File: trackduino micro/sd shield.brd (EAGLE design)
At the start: 43.7 x 19.6 mm, 12 parts, among them U1 FT232RL-BASICSSOP

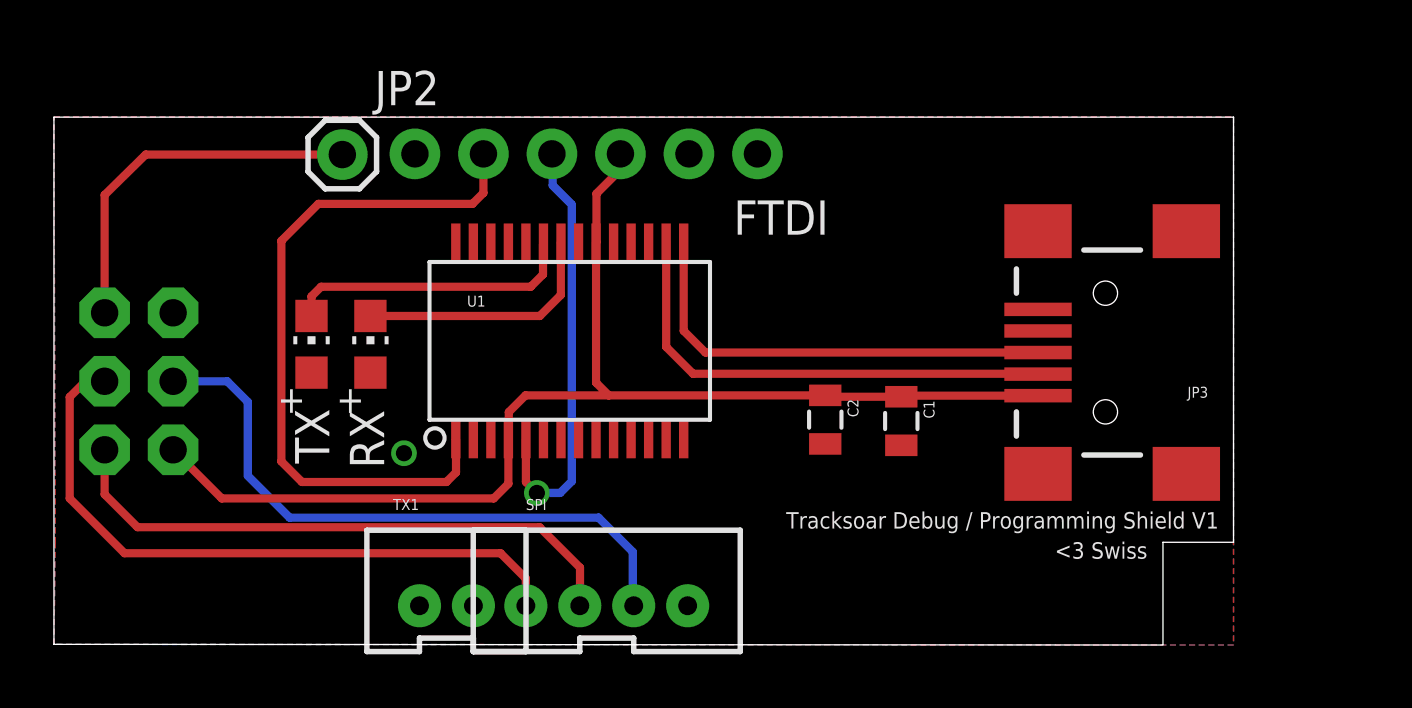
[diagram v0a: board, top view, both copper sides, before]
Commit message: Shield Updates
added sd storage shield, added fetid chip to programming shield. Moved
test boards to correct folder.
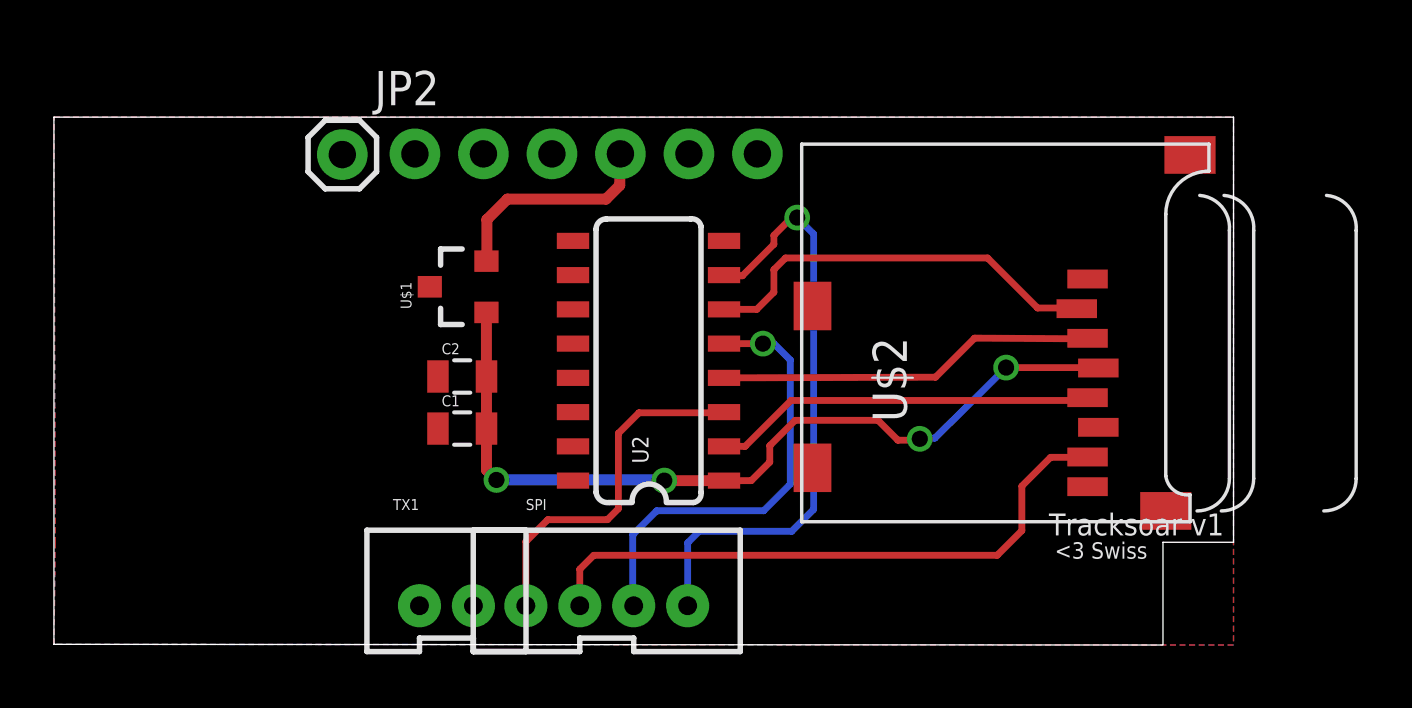
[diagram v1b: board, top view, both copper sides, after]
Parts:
- removed ICSP: AVR_SPI_PRG_6PTH, SparkFun-Connectors:2X3
- removed JP3: USBSMD, SparkFun-Connectors:USB-MINIB
- removed RX, TX: (no value), adafruit:CHIP-LED0805
- removed U1: FT232RL-BASICSSOP, SparkFun-DigitalIC:SSOP28DB
- added U$1: LM3480IM4, SparkFun-PowerIC:SOT23-3
- added U$2: MICROSD, adafruit:MICROSD
- added U2: HEX_CONVERTER, SparkFun-DigitalIC:SO016
- C2: value 100pf -> .1uf
- moved C1 16.3 mm to (14.7, 7.67), turned to 0 degrees
- moved C2 13.6 mm to (14.7, 9.60), turned to 0 degrees
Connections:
- removed net RXLED: RX.C, U1.22
- removed net TXLED: TX.C, U1.23
- removed net USBDM: JP3.D-, U1.16
- removed net USBDP: JP3.D+, U1.15
- new net 3V: C1.2, C2.2, U$1.1, U$2.4, U2.1
- new net CS: U$2.2, U2.6
- new net DI: U$2.3, U2.4
- new net SCLK: U$2.5, U2.2
- net !RESET: no longer ICSP.5
- net GND: now also C1.1, C2.1, U$1.3, U$2.6, U$2.MT1, U$2.MT2, U2.11, U2.14, U2.8, U2.9; no longer C1.2, C2.2, ICSP.6, JP3.GND, RX.A, TX.A, U1.11, U1.18, U1.2, U1.21, U1.25, U1.26, U1.3, U1.7
- net MISO: now also U$2.7; no longer ICSP.1
- net MOSI: now also U2.5; no longer ICSP.4
- net RXO: no longer U1.1
- net SCK: now also U2.3; no longer ICSP.3
- net SS: now also U2.7
- net TXO: no longer U1.5
- net VCC: now also U$1.2; no longer C1.1, C2.1, ICSP.2, JP3.VBUS, U1.20, U1.4
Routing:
- net VCC: track 45.5 -> 8.18 mm
- net 3V: track 0.00 -> 31.4 mm, vias 0 -> 4
- net RXO: track 26.0 -> 0.00 mm
- net SS: track 0.00 -> 22.4 mm, vias 0 -> 1
- net USBDM: track 18.1 -> 0.00 mm
- net USBDP: track 16.8 -> 0.00 mm
- net TXO: track 16.1 -> 0.00 mm, vias 1 -> 0
- net CS: track 0.00 -> 15.1 mm
- net SCLK: track 0.00 -> 14.2 mm
- net DI: track 0.00 -> 14.1 mm
- net !RESET: track 13.8 -> 0.00 mm
- net SCK: track 24.4 -> 13.4 mm
- net TXLED: track 10.8 -> 0.00 mm
- net RXLED: track 9.34 -> 0.00 mm
- net MOSI: track 23.3 -> 16.6 mm, vias 0 -> 1
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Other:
- board text added: "Tracksoar v1"
- board text removed: "Tracksoar Debug / Programming Shield V1"
